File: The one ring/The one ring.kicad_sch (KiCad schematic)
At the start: 5 parts, among them J1 LiPo_100-150mAh, SW1 SW_Push, U1 XIAO-ESP32-S3-Sense, U2 MAX98357A

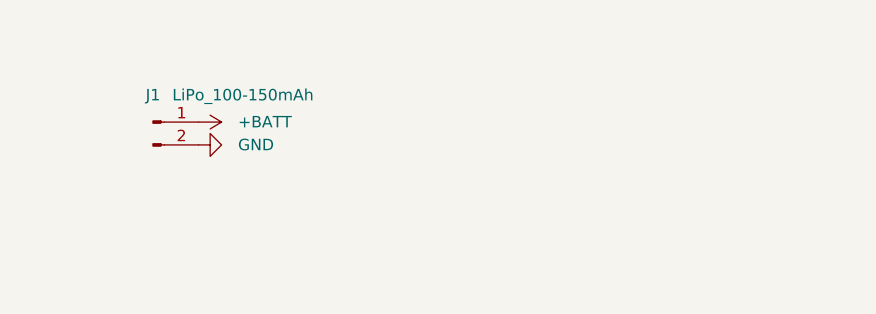
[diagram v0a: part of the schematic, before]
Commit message: Add +BATT note and update PCB footprints
Add schematic note documenting +BATT connects to XIAO onboard JST.
Update PCB with latest custom MAX98357A breakout footprint changes.

Co-Authored-By: Claude Sonnet 4.6 <noreply@anthropic.com>
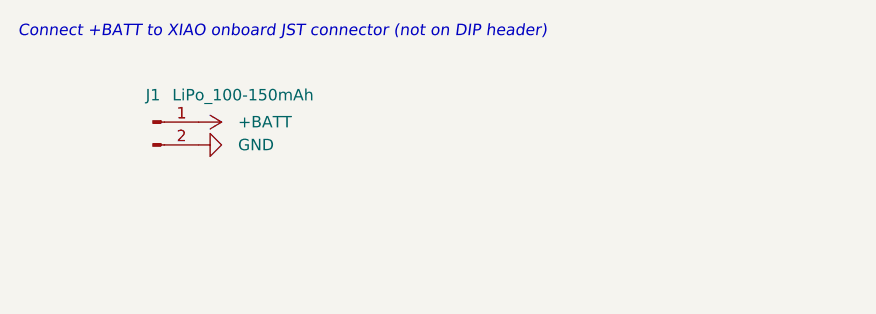
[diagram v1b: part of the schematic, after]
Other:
- note added: "Connect +BATT to XIAO onboard JST connector (not on DIP header)"
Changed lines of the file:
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@@
 	(generator_version "10.0")
 	(paper "A4")
+	(text "Connect +BATT to XIAO onboard JST connector (not on DIP header)"
+		(at 20 65 0)
+		(effects
+			(font
+				(size 1.27 1.27)
+				(italic yes)
+			)
+			(justify left)
+		)
+	)
 	(no_connect
 		(at 97.46 124.13)
